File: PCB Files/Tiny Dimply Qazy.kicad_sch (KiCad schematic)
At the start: 26 parts, among them J1 Conn_01x04_Male, J2 USB_C_Receptacle_USB2.0, Q1 2N7002, SW1 B/R, U1 STM32F072CBTx, U2 XC6206PxxxMR-Regulator_Linear, U3 USBLC6-2SC6

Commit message: Add prototype production changes
* R4, R5 to 0603 (as requested during prototype PCBA)
* Replace C_VDD2 with C_VDD3
* Add missing ground connections for R1, R2
* Move silk texts to the back
* Centered big silk text
* Add Molex EZMate Pico 4-pin header close to the JST SH header
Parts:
- removed C_VDD2: 100n, Capacitor_SMD:C_0603_1608Metric, symbol Device:C_Small
- added J3: Conn_01x04_Male, Connector_Molex:Molex_Pico-EZmate_78171-0004_1x04-1MP_P1.20mm_Vertical, symbol Connector_Generic_MountingPin:Conn_01x04_MountingPin
- renumbered C_VDD3 to C_VDD2
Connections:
- net +5V: now also J3.1 (Pin_1)
- net DBUS+: now also J3.3 (Pin_3)
- net DBUS-: now also J3.2 (Pin_2)
- net GND: now also J3.4 (Pin_4), J3.MP (MountPin)
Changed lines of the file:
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@@
   (junction (at 86.995 182.88) (diameter 0) (color 0 0 0 0)
   )
-  (junction (at 61.595 170.18) (diameter 0) (color 0 0 0 0)
-  )
   (junction (at 149.352 104.267) (diameter 0.9144) (color 0 0 0 0)
   )
@@
   (junction (at 202.946 102.87) (diameter 0.9144) (color 0 0 0 0)
   )
-  (junction (at 61.595 165.1) (diameter 0) (color 0 0 0 0)
-  )
   (junction (at 65.913 103.124) (diameter 0) (color 0 0 0 0)
   )
+  (junction (at 184.404 124.968) (diameter 0) (color 0 0 0 0)
+  )
   (junction (at 68.453 103.124) (diameter 0) (color 0 0 0 0)
   )
@@
   )
   (junction (at 95.123 90.424) (diameter 0) (color 0 0 0 0)
+  )
+  (junction (at 150.876 150.622) (diameter 0) (color 0 0 0 0)
   )
   (junction (at 68.453 26.924) (diameter 0) (color 0 0 0 0)
@@
     (stroke (width 0) (type solid) (color 0 0 0 0))
   )
+  (bus (pts (xy 150.876 150.622) (xy 184.404 150.622))
+    (stroke (width 0) (type default) (color 0 0 0 0))
+  )
   (wire (pts (xy 237.109 46.355) (xy 248.539 46.355))
     (stroke (width 0) (type default) (color 0 0 0 0))
@@
     (stroke (width 0) (type default) (color 0 0 0 0))
   )
+  (bus (pts (xy 184.404 124.968) (xy 190.246 124.968))
+    (stroke (width 0) (type default) (color 0 0 0 0))
+  )
   (wire (pts (xy 127.762 17.145) (xy 128.524 17.145))
     (stroke (width 0) (type default) (color 0 0 0 0))
@@
     (stroke (width 0) (type default) (color 0 0 0 0))
   )
+  (bus (pts (xy 150.876 124.968) (xy 150.876 150.622))
+    (stroke (width 0) (type default) (color 0 0 0 0))
+  )
   (wire (pts (xy 156.972 115.697) (xy 164.592 115.697))
     (stroke (width 0) (type default) (color 0 0 0 0))
   )
-  (wire (pts (xy 74.295 165.1) (xy 61.595 165.1))
+  (wire (pts (xy 48.895 165.1) (xy 74.295 165.1))
     (stroke (width 0) (type default) (color 0 0 0 0))
   )
@@
     (stroke (width 0) (type solid) (color 0 0 0 0))
   )
-  (bus (pts (xy 150.876 150.622) (xy 150.876 124.968))
-    (stroke (width 0) (type default) (color 0 0 0 0))
-  )
   (wire (pts (xy 137.922 113.157) (xy 137.922 115.697))
     (stroke (width 0) (type solid) (color 0 0 0 0))
@@
     (stroke (width 0) (type default) (color 0 0 0 0))
   )
-  (wire (pts (xy 74.295 170.18) (xy 61.595 170.18))
+  (wire (pts (xy 48.895 170.18) (xy 74.295 170.18))
     (stroke (width 0) (type default) (color 0 0 0 0))
   )
@@
     (stroke (width 0) (type solid) (color 0 0 0 0))
   )
-  (wire (pts (xy 61.595 170.18) (xy 48.895 170.18))
-    (stroke (width 0) (type default) (color 0 0 0 0))
-  )
   (wire (pts (xy 86.995 157.48) (xy 61.595 157.48))
     (stroke (width 0) (type default) (color 0 0 0 0))
@@
     (stroke (width 0) (type default) (color 0 0 0 0))
   )
-  (wire (pts (xy 48.895 165.1) (xy 61.595 165.1))
-    (stroke (width 0) (type default) (color 0 0 0 0))
-  )
   (wire (pts (xy 194.945 44.323) (xy 196.342 44.323))
     (stroke (width 0) (type default) (color 0 0 0 0))
@@
     (stroke (width 0) (type solid) (color 0 0 0 0))
   )
-  (bus (pts (xy 150.876 124.968) (xy 190.246 124.968))
+  (bus (pts (xy 150.876 124.968) (xy 184.404 124.968))
+    (stroke (width 0) (type default) (color 0 0 0 0))
+  )
+  (bus (pts (xy 184.404 150.622) (xy 184.404 124.968))
     (stroke (width 0) (type default) (color 0 0 0 0))
   )
@@
     )
   )
+  (global_label "DBUS+" (shape input) (at 165.227 136.398 180) (fields_autoplaced)
+    (effects (font (size 1.27 1.27)) (justify right))
+    (property "Intersheet References" "${INTERSHEET_REFS}" (id 0) (at 156.1615 136.4774 0)
+      (effects (font (size 1.27 1.27)) (justify right) hide)
+    )
+  )
   (global_label "NRST" (shape output) (at 167.132 99.187 0) (fields_autoplaced)
     (effects (font (size 1.27 1.27)) (justify left))
@@
     (property "Intersheet References" "${INTERSHEET_REFS}" (id 0) (at 136.7912 38.1476 0)
       (effects (font (size 1.27 1.27)) (justify left) hide)
+    )
+  )
+  (global_label "DBUS-" (shape input) (at 165.227 133.858 180) (fields_autoplaced)
+    (effects (font (size 1.27 1.27)) (justify right))
+    (property "Intersheet References" "${INTERSHEET_REFS}" (id 0) (at 156.1615 133.9374 0)
+      (effects (font (size 1.27 1.27)) (justify right) hide)
     )
   )
@@
     )
     (property "Datasheet" "" (id 3) (at 131.699 138.938 0)
+      (effects (font (size 1.27 1.27)) hide)
+    )
+    (pin "1")
+  )
+  (symbol (lib_id "power:+5V") (at 165.227 131.318 0) (unit 1)
+    (in_bom yes) (on_board yes) (fields_autoplaced)
+    (property "Reference" "#PWR0102" (id 0) (at 165.227 135.128 0)
+      (effects (font (size 1.27 1.27)) hide)
+    )
+    (property "Value" "+5V" (id 1) (at 165.227 127.7422 0))
+    (property "Footprint" "" (id 2) (at 165.227 131.318 0)
+      (effects (font (size 1.27 1.27)) hide)
+    )
+    (property "Datasheet" "" (id 3) (at 165.227 131.318 0)
       (effects (font (size 1.27 1.27)) hide)
     )
@@
     (pin "1")
   )
+  (symbol (lib_id "power:GND") (at 170.307 144.018 0) (unit 1)
+    (in_bom yes) (on_board yes) (fields_autoplaced)
+    (property "Reference" "#PWR0103" (id 0) (at 170.307 150.368 0)
+      (effects (font (size 1.27 1.27)) hide)
+    )
+    (property "Value" "GND" (id 1) (at 170.307 148.4614 0))
+    (property "Footprint" "" (id 2) (at 170.307 144.018 0)
+      (effects (font (size 1.27 1.27)) hide)
+    )
+    (property "Datasheet" "" (id 3) (at 170.307 144.018 0)
+      (effects (font (size 1.27 1.27)) hide)
+    )
+    (pin "1")
+  )
   (symbol (lib_id "Device:Polyfuse_Small") (at 203.073 23.241 270) (unit 1)
     (in_bom yes) (on_board yes)
@@
     (pin "2")
   )
+  (symbol (lib_id "Connector_Generic_MountingPin:Conn_01x04_MountingPin") (at 170.307 133.858 0) (unit 1)
+    (in_bom yes) (on_board yes)
+    (property "Reference" "J3" (id 0) (at 170.942 127.542 0))
+    (property "Value" "Conn_01x04_Male" (id 1) (at 172.847 129.921 0))
+    (property "Footprint" "Connector_Molex:Molex_Pico-EZmate_78171-0004_1x04-1MP_P1.20mm_Vertical" (id 2) (at 170.307 133.858 0)
+      (effects (font (size 1.27 1.27)) hide)
+    )
+    (property "Datasheet" "~" (id 3) (at 170.307 133.858 0)
+      (effects (font (size 1.27 1.27)) hide)
+    )
+    (pin "1")
+    (pin "2")
+    (pin "3")
+    (pin "4")
+    (pin "MP")
+  )
   (symbol (lib_id "power:GND") (at 86.995 182.88 0) (unit 1)
     (in_bom yes) (on_board yes)
@@
     (pin "1")
   )
-  (symbol (lib_id "Device:C_Small") (at 61.595 167.64 0) (unit 1)
-    (in_bom yes) (on_board yes)
-    (property "Reference" "C_VDD2" (id 0) (at 63.9318 166.4716 0)
-      (effects (font (size 1.27 1.27)) (justify left))
-    )
-    (property "Value" "100n" (id 1) (at 63.9318 168.783 0)
-      (effects (font (size 1.27 1.27)) (justify left))
-    )
-    (property "Footprint" "Capacitor_SMD:C_0603_1608Metric" (id 2) (at 61.595 167.64 0)
-      (effects (font (size 1.27 1.27)) hide)
-    )
-    (property "Datasheet" "~" (id 3) (at 61.595 167.64 0)
-      (effects (font (size 1.27 1.27)) hide)
-    )
-    (pin "1")
-    (pin "2")
-  )
   (symbol (lib_id "power:+5V") (at 131.699 131.318 0) (unit 1)
     (in_bom yes) (on_board yes) (fields_autoplaced)
@@
   (symbol (lib_id "Device:C_Small") (at 74.295 167.64 0) (unit 1)
     (in_bom yes) (on_board yes)
-    (property "Reference" "C_VDD3" (id 0) (at 76.6318 166.4716 0)
+    (property "Reference" "C_VDD2" (id 0) (at 76.6318 166.4716 0)
       (effects (font (size 1.27 1.27)) (justify left))
     )
@@
     (pin "2")
   )
+  (symbol (lib_id "power:GND") (at 165.227 138.938 0) (unit 1)
+    (in_bom yes) (on_board yes) (fields_autoplaced)
+    (property "Reference" "#PWR0101" (id 0) (at 165.227 145.288 0)
+      (effects (font (size 1.27 1.27)) hide)
+    )
+    (property "Value" "GND" (id 1) (at 165.227 143.3814 0))
+    (property "Footprint" "" (id 2) (at 165.227 138.938 0)
+      (effects (font (size 1.27 1.27)) hide)
+    )
+    (property "Datasheet" "" (id 3) (at 165.227 138.938 0)
+      (effects (font (size 1.27 1.27)) hide)
+    )
+    (pin "1")
+  )
   (sheet (at 117.348 55.753) (size 38.354 28.956) (fields_autoplaced)
     (stroke (width 0.1524) (type solid) (color 0 0 0 0))
@@
       (reference "#PWR023") (unit 1) (value "+5V") (footprint "")
     )
+    (path "/ff274ac6-dc19-4e64-b217-9830a6656d17"
+      (reference "#PWR0101") (unit 1) (value "GND") (footprint "")
+    )
+    (path "/0ca329db-4977-4260-a415-8434c9fbfb9e"
+      (reference "#PWR0102") (unit 1) (value "+5V") (footprint "")
+    )
+    (path "/51b5fd8d-c952-4883-94b2-bc863b76b02c"
+      (reference "#PWR0103") (unit 1) (value "GND") (footprint "")
+    )
     (path "/e940c989-d5b1-4a34-84a5-dd381089618c"
       (reference "C1") (unit 1) (value "4.7uF") (footprint "Capacitor_SMD:C_0402_1005Metric")
@@
       (reference "C_VDD1") (unit 1) (value "100n") (footprint "Capacitor_SMD:C_0603_1608Metric")
     )
-    (path "/63a97909-7362-4099-8075-dab92792347b"
-      (reference "C_VDD2") (unit 1) (value "100n") (footprint "Capacitor_SMD:C_0603_1608Metric")
-    )
     (path "/6d2af29e-9c90-4891-ab51-f083ce6ae2c4"
-      (reference "C_VDD3") (unit 1) (value "4.7u") (footprint "Capacitor_SMD:C_0603_1608Metric")
+      (reference "C_VDD2") (unit 1) (value "4.7u") (footprint "Capacitor_SMD:C_0603_1608Metric")
     )
     (path "/beaec504-2202-403a-a0c3-6cd86ed50f84"
@@
       (reference "J2") (unit 1) (value "USB_C_Receptacle_USB2.0") (footprint "Connector_USB:USB_C_Receptacle_HRO_TYPE-C-31-M-12")
     )
+    (path "/5745152b-2b5f-4ccd-a4d6-daff222c82af"
+      (reference "J3") (unit 1) (value "Conn_01x04_Male") (footprint "Connector_Molex:Molex_Pico-EZmate_78171-0004_1x04-1MP_P1.20mm_Vertical")
+    )
     (path "/e05344b5-a96e-4473-b41e-e9f45716bf1d/49e638fb-f500-4a8f-9f71-7b4b5947b0dc"

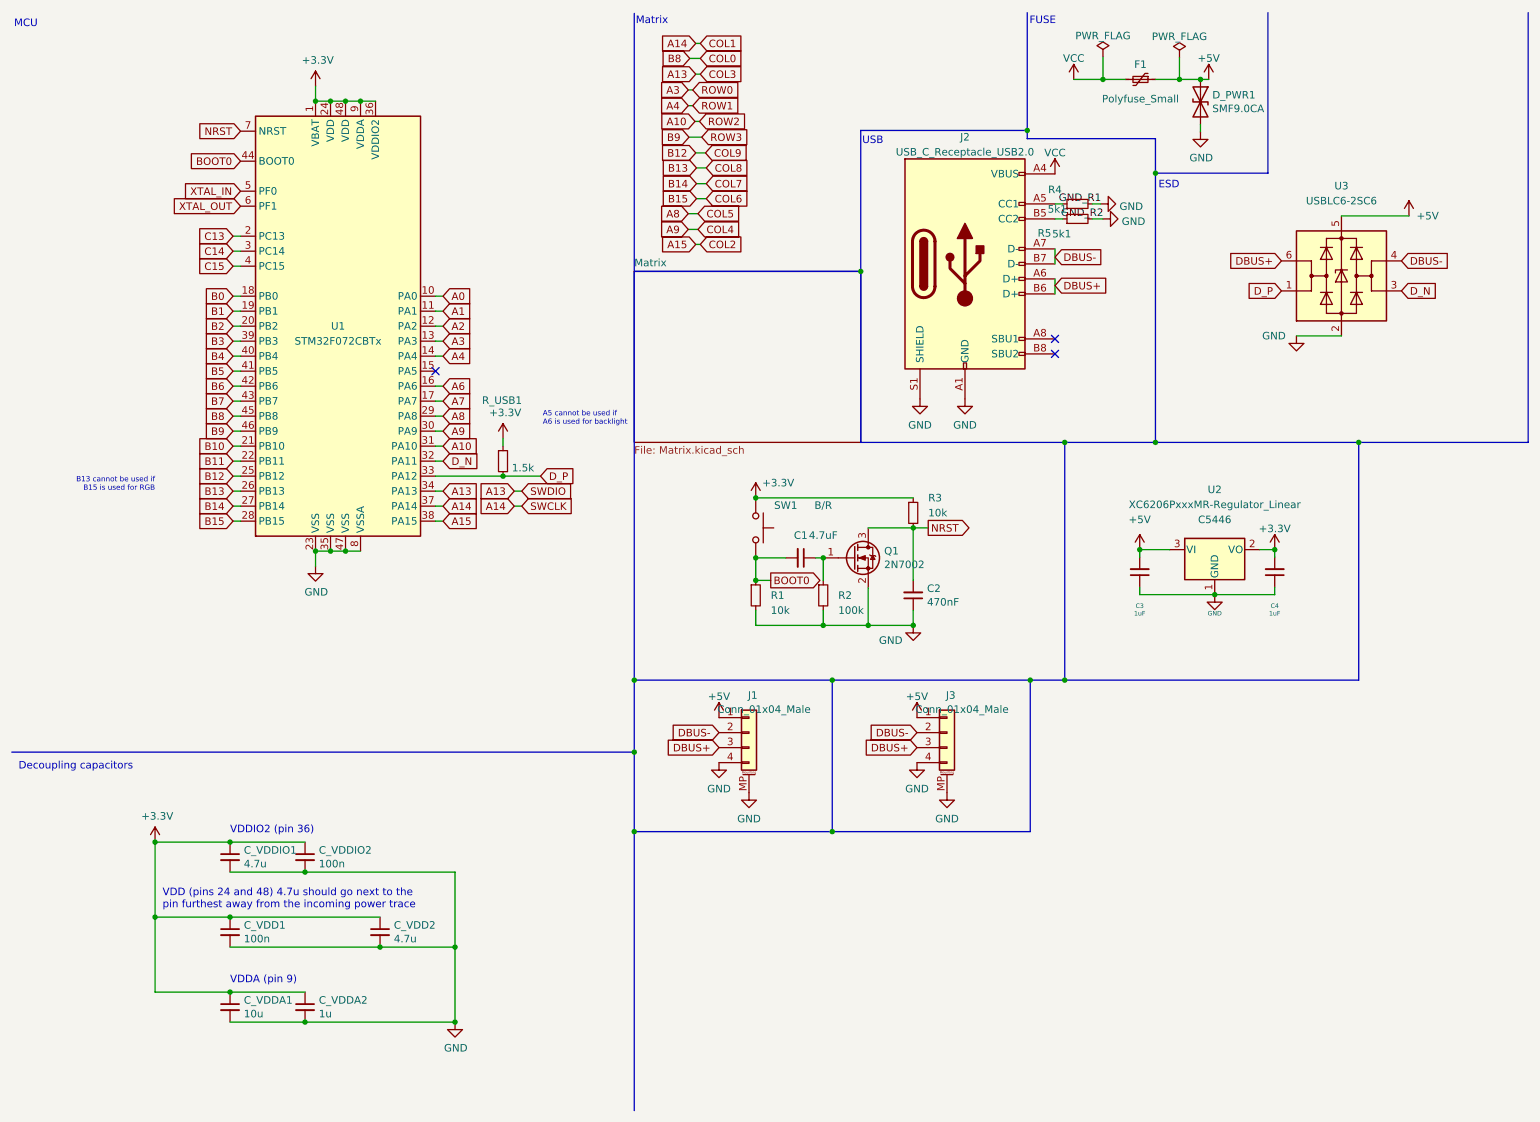
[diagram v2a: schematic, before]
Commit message: Cleanup the schematics and add a library for smaller bav70s
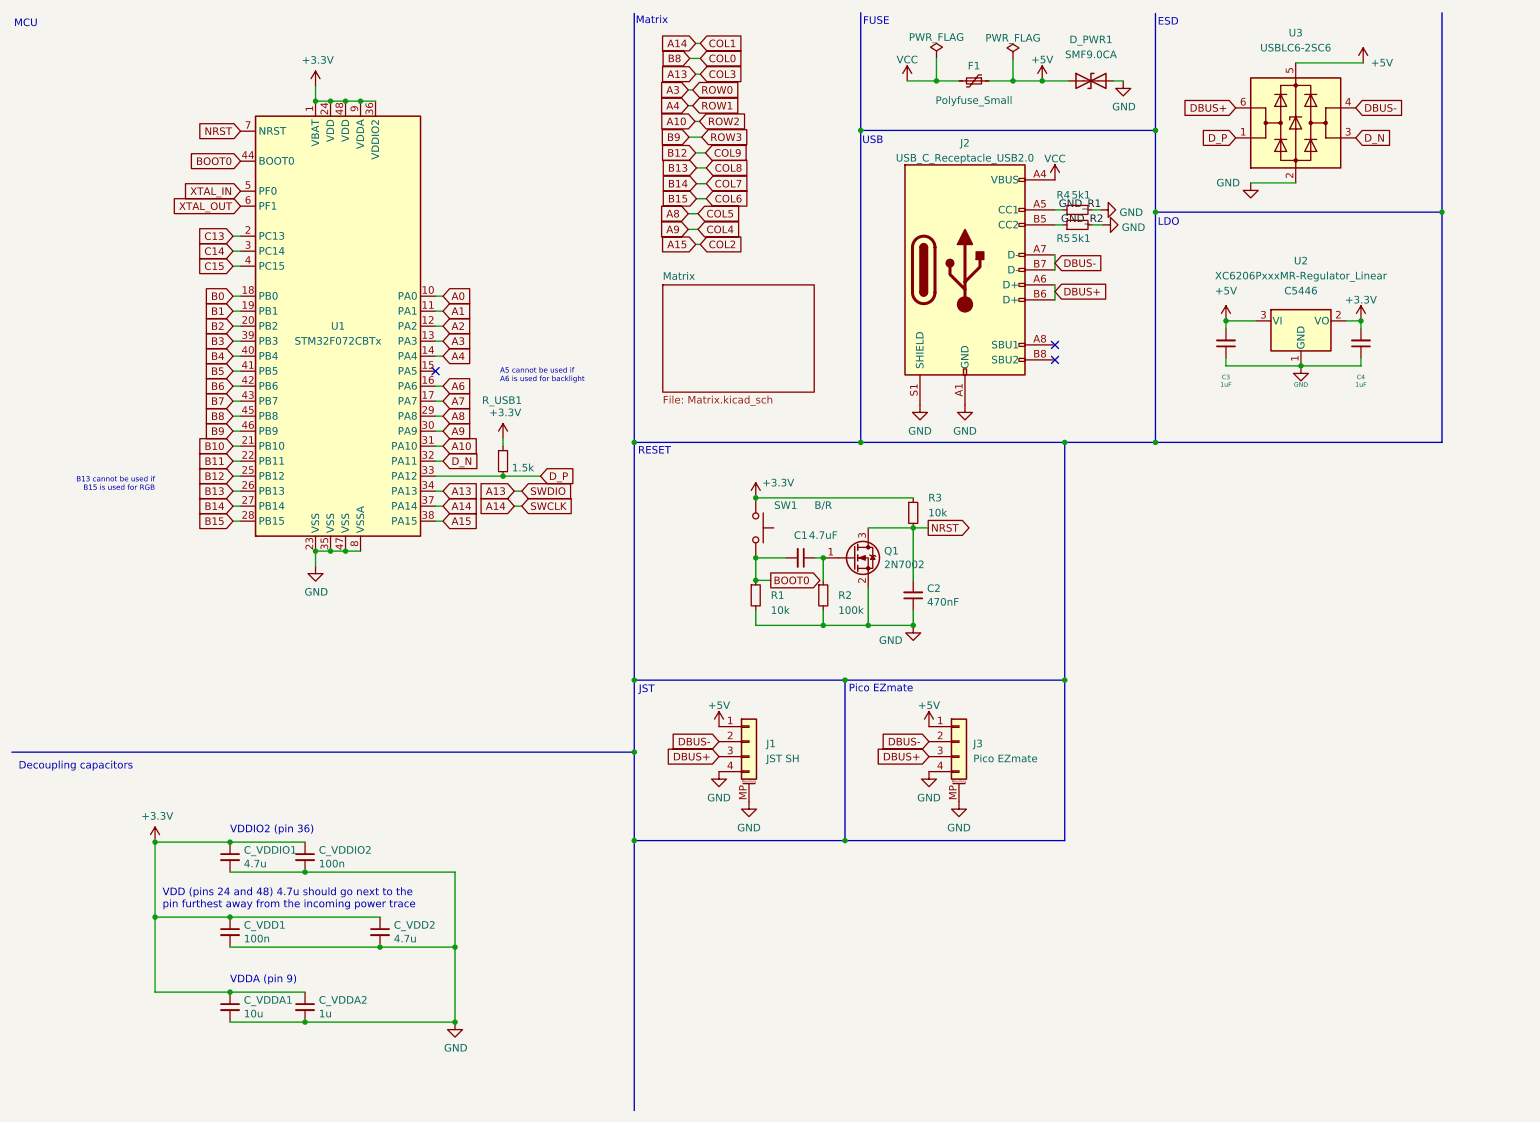
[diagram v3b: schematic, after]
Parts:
- J1: value Conn_01x04_Male -> JST SH
- J3: value Conn_01x04_Male -> Pico EZmate
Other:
- note added: "JST"
- note added: "LDO"
- note added: "Pico EZmate"
- note added: "RESET"
- moved on the sheet: C3, C4, D_PWR1, F1, J1, J2, J3, R4, R5, U2, U3

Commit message: Update dump
- Fix bottom row layout
- Add copium to dubba 1.75u shift using 1.5u and 1.25u
- Uglify @ASH-ART's routing
- Generate gerbers as recommended by JLC
- Add a logotype and revision number
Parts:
- C_VDD1, C_VDD2, C_VDDIO2: LCSC (none) -> C14663
- C_VDDA1: LCSC (none) -> C19702
- C_VDDA2: LCSC (none) -> C15849
- C_VDDIO1: LCSC (none) -> C19666
- D_PWR1: LCSC (none) -> C123799
- F1: LCSC (none) -> C10677
- J1: LCSC (none) -> C2845363
- J2: LCSC (none) -> C2765186
- J3: LCSC (none) -> C588524
- R4, R5: LCSC (none) -> C83063
- R_USB1: LCSC (none) -> C22843
- U1: LCSC (none) -> C81720
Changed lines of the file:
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@@
+      (effects (font (size 1.27 1.27)) hide)
+    )
+    (property "LCSC" "C2845363" (id 4) (at 139.7 135.7375 0)
       (effects (font (size 1.27 1.27)) hide)
     )
@@
     )
     (property "Datasheet" "~" (id 3) (at 61.595 154.94 0)
+      (effects (font (size 1.27 1.27)) hide)
+    )
+    (property "LCSC" "C14663" (id 4) (at 63.9318 153.7716 0)
       (effects (font (size 1.27 1.27)) hide)
     )
@@
       (effects (font (size 1.27 1.27)) hide)
     )
+    (property "LCSC" "C10677" (id 4) (at 174.879 20.955 0)
+      (effects (font (size 1.27 1.27)) hide)
+    )
     (pin "1")
     (pin "2")
@@
     )
     (property "Datasheet" "~" (id 3) (at 172.339 135.382 0)
+      (effects (font (size 1.27 1.27)) hide)
+    )
+    (property "LCSC" "C588524" (id 4) (at 174.752 135.7375 0)
       (effects (font (size 1.27 1.27)) hide)
     )
@@
       (effects (font (size 1.27 1.27)) hide)
     )
+    (property "LCSC" "C14663" (id 4) (at 51.2318 166.4716 0)
+      (effects (font (size 1.27 1.27)) hide)
+    )
     (pin "1")
     (pin "2")
@@
     )
     (property "Datasheet" "~" (id 3) (at 74.295 167.64 0)
+      (effects (font (size 1.27 1.27)) hide)
+    )
+    (property "LCSC" "C14663" (id 4) (at 76.6318 166.4716 0)
       (effects (font (size 1.27 1.27)) hide)
     )
@@
     )
     (property "Datasheet" "http://www.st.com/st-web-ui/static/active/en/resource/technical/document/datasheet/DM00090510.pdf" (id 3) (at 68.453 65.024 0)
+      (effects (font (size 1.27 1.27)) hide)
+    )
+    (property "LCSC" "C81720" (id 4) (at 67.183 65.024 0)
       (effects (font (size 1.27 1.27)) hide)
     )
@@
       (effects (font (size 1.27 1.27)) hide)
     )
+    (property "LCSC" "C83063" (id 4) (at 188.849 43.561 0)
+      (effects (font (size 1.27 1.27)) hide)
+    )
     (pin "1")
     (pin "2")
@@
     )
     (property "Datasheet" "~" (id 3) (at 48.895 180.34 0)
+      (effects (font (size 1.27 1.27)) hide)
+    )
+    (property "LCSC" "C19702" (id 4) (at 51.2318 179.1716 0)
       (effects (font (size 1.27 1.27)) hide)
     )
@@
     )
     (property "Datasheet" "https://www.usb.org/sites/default/files/documents/usb_type-c.zip" (id 3) (at 177.165 55.499 0)
+      (effects (font (size 1.27 1.27)) hide)
+    )
+    (property "LCSC" "C2765186" (id 4) (at 173.355 34.0192 0)
       (effects (font (size 1.27 1.27)) hide)
     )
@@
       (effects (font (size 1.27 1.27)) hide)
     )
+    (property "LCSC" "C123799" (id 4) (at 194.691 16.51 0)
+      (effects (font (size 1.27 1.27)) hide)
+    )
     (pin "1")
     (pin "2")
@@
     )
     (property "Datasheet" "~" (id 3) (at 95.123 87.884 0)
+      (effects (font (size 1.27 1.27)) hide)
+    )
+    (property "LCSC" "C22843" (id 4) (at 91.567 77.597 0)
       (effects (font (size 1.27 1.27)) hide)
     )
@@
       (effects (font (size 1.27 1.27)) hide)
     )
+    (property "LCSC" "C15849" (id 4) (at 63.9318 179.1716 0)
+      (effects (font (size 1.27 1.27)) hide)
+    )
     (pin "1")
     (pin "2")
@@
     )
     (property "Datasheet" "~" (id 3) (at 48.895 154.94 0)
+      (effects (font (size 1.27 1.27)) hide)
+    )
+    (property "LCSC" "C19666" (id 4) (at 51.2318 153.7716 0)
       (effects (font (size 1.27 1.27)) hide)
     )
@@
     )
     (property "Datasheet" "~" (id 3) (at 192.405 47.879 0)
+      (effects (font (size 1.27 1.27)) hide)
+    )
+    (property "LCSC" "C83063" (id 4) (at 188.849 50.165 0)
       (effects (font (size 1.27 1.27)) hide)
     )
@@
       (reference "MX44") (unit 1) (value "MX-NoLED") (footprint "MX_Only:MXOnly-1.75U-NoLED")
     )
+    (path "/e05344b5-a96e-4473-b41e-e9f45716bf1d/cd5dd937-3321-4f9e-b98f-f820b15bf16b"
+      (reference "MX45") (unit 1) (value "MX-NoLED") (footprint "MX_Only:MXOnly-1.5U-NoLED")
+    )
+    (path "/e05344b5-a96e-4473-b41e-e9f45716bf1d/af140b2a-6001-4acf-b489-6480e74ca516"
+      (reference "MX46") (unit 1) (value "MX-NoLED") (footprint "MX_Only:MXOnly-1.25U-NoLED")
+    )
+    (path "/e05344b5-a96e-4473-b41e-e9f45716bf1d/85edf8ea-b83b-4ed4-96d1-56cb851eab3f"
+      (reference "MX47") (unit 1) (value "MX-NoLED") (footprint "MX_Only:MXOnly-1.25U-NoLED")
+    )
+    (path "/e05344b5-a96e-4473-b41e-e9f45716bf1d/152d111d-4aa2-407a-9930-b6e2b0135b39"
+      (reference "MX48") (unit 1) (value "MX-NoLED") (footprint "MX_Only:MXOnly-1.5U-NoLED")
+    )
     (path "/6d17ae96-61ae-4dbf-8cb4-81d9fbfa6b9a"
